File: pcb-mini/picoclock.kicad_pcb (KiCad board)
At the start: 2 copper layers, 140 x 54 mm, 123 parts, among them J1 UART, J10 USB, J11 Alt Power, J12 LED_5V, J14 SM03B-SRSS-TB, J15 Conn_01x24, J2 USB_A, J4 xx, J5 Micro_SD_Card_Det1, J6 USB_C_Receptacle, J9 AUDIO, Q1 BSS138, Q3 BSS138, SW1 SW_Push, SW2 SW_Push, SW3 SW_Push, SW4 SW_Push, SW5 SW_Push, SW6 SW_Push, SW7 SW_Push, SW8 SW_Push, U1 PCF8563T, U2 RP2350_80QFN, U3 MCP9808_MSOP, U4 PCM5100, U5 PAM8302A, U7 MCP45X1-104E, U8 NCP1117-3.3_SOT223, U9 ESP32-WROOM-E, Y1 Crystal, Y2 ABM8-272-T3

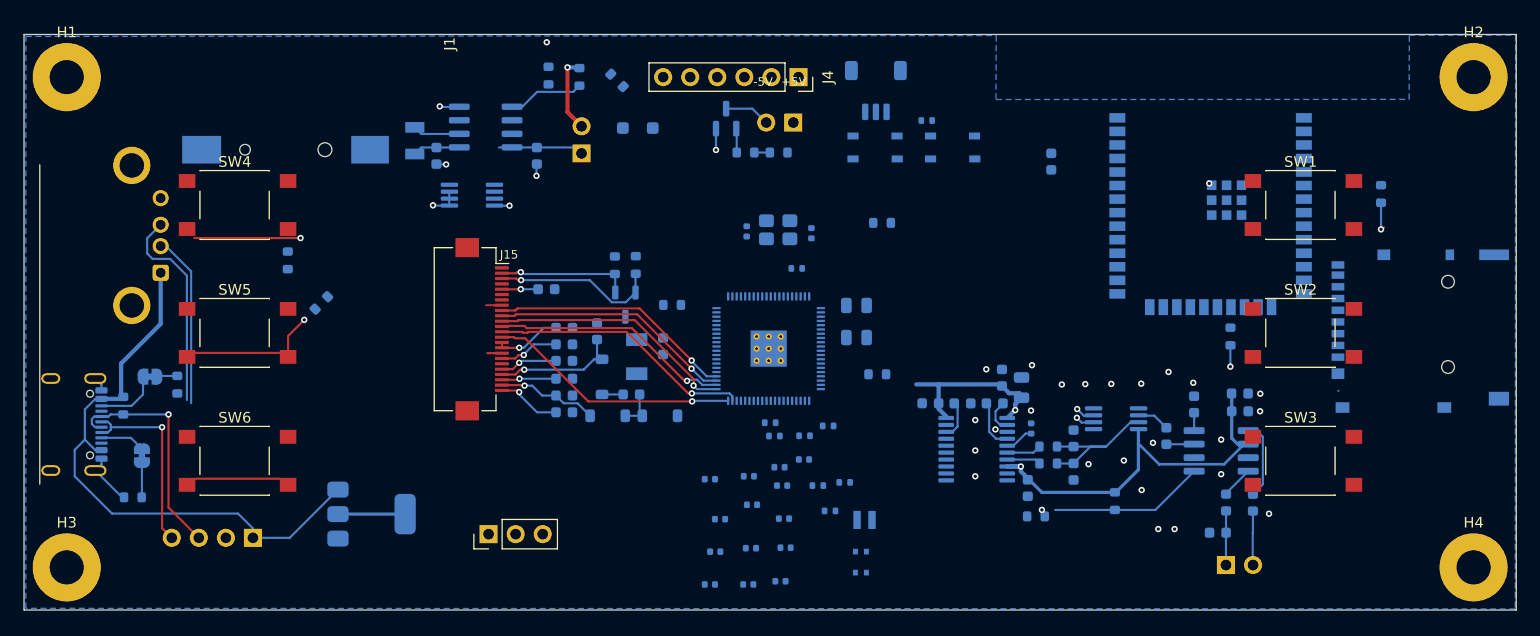
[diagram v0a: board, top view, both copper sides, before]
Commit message: [pcb-mini] add ESP32, RM2, route most things
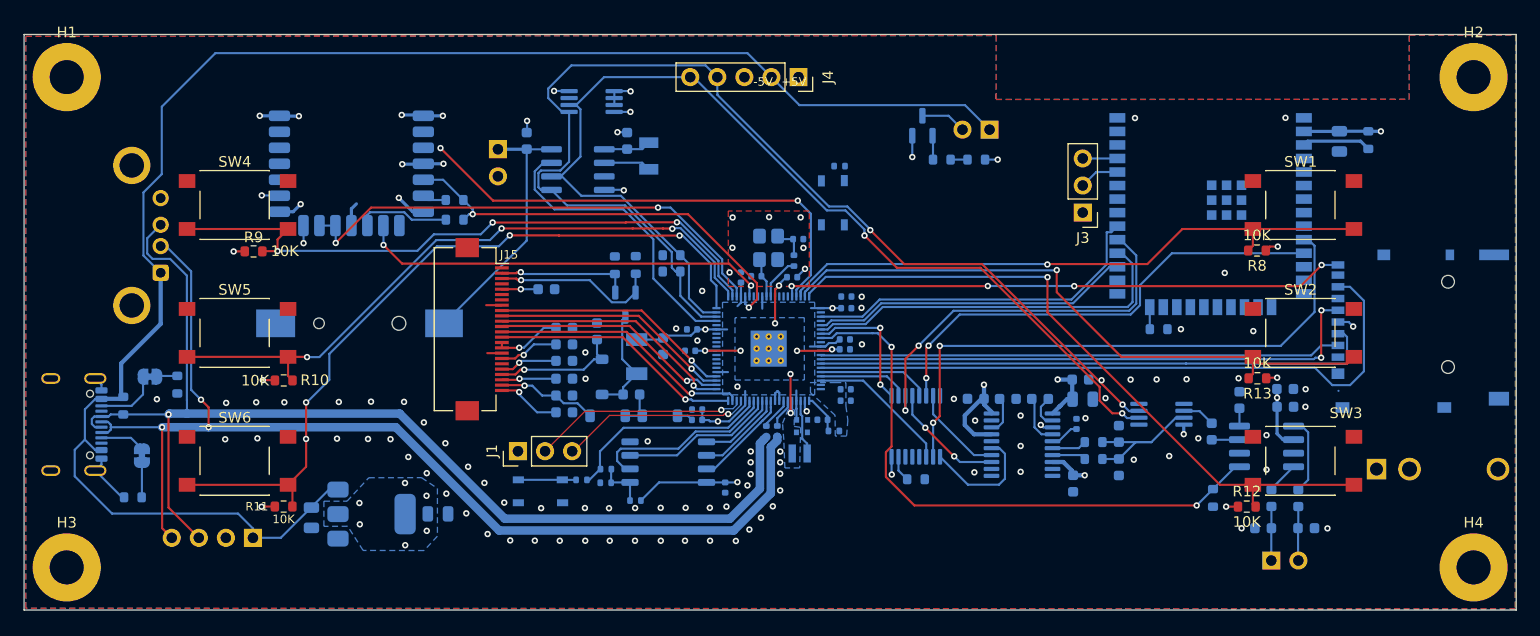
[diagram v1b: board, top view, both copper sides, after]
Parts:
- removed D1: 1A 20V Schottky, Diode_SMD:D_SOD-123F
- removed J14: SM03B-SRSS-TB, Connector_JST:JST_SH_SM03B-SRSS-TB_1x03-1MP_P1.00mm_Horizontal
- removed the R1 at (132.1, 84.0)
- removed the R17 at (160.5, 97.7)
- removed the R17 at (150.8, 91.1)
- removed the R3 at (135.6, 84.3)
- added C48: 10u, Capacitor_SMD:C_0805_2012Metric, B.Cu at (203.4, 90.0)
- added J3: UART, Connector_PinHeader_2.54mm:PinHeader_1x03_P2.54mm_Vertical, F.Cu at (179.3, 96.7)
- added J7: AudioJack2_Ground, Connector_Audio:Jack_3.5mm_QingPu_WQP-PJ398SM_Vertical_CircularHoles, B.Cu at (206.9, 120.8)
- added J8: Conn_01x21_Pin, RMC20452T:RMC20452T, B.Cu at (110.7, 90.2)
- added R17: 10K, Resistor_SMD:R_0603_1608Metric, B.Cu at (169.3, 91.7)
- added R28: 10K, Resistor_SMD:R_0603_1608Metric, B.Cu at (186.4, 107.7)
- added R29: 10K, Resistor_SMD:R_0603_1608Metric, B.Cu at (206.1, 89.9)
- added R30: 10K, Resistor_SMD:R_0603_1608Metric, B.Cu at (163.7, 121.7)
- added R37: 470, Resistor_SMD:R_0603_1608Metric, B.Cu at (120.4, 95.5)
- added R38: 10k, Resistor_SMD:R_0603_1608Metric, B.Cu at (120.4, 97.4)
- added U10: 74LS157, Package_SO:TSSOP-16_4.4x5mm_P0.65mm, B.Cu at (163.7, 116.8)
- added U6: W25Q128JVS, Package_SO:SOIC-8_5.3x5.3mm_P1.27mm, B.Cu at (140.4, 120.1)
- J4: footprint Connector_PinSocket_2.54mm:PinSocket_1x06_P2.54mm_Vertical -> Connector_PinSocket_2.54mm:PinSocket_1x05_P2.54mm_Vertical
- R10, R11, R12, R13, R8, R9: moved to F.Cu
- moved C46 53.9 mm to (107.0, 125.3), turned to -90 degrees
- moved SW7 50.4 mm to (128.4, 122.9)
- moved R11 47.5 mm to (104.3, 124.3), turned to 0 degrees
- moved R15 46.8 mm to (132.3, 121.8), turned to 180 degrees
- moved C47 43.9 mm to (118.8, 125.0)
- moved C30 41.9 mm to (200.3, 126.3), turned to 0 degrees
- moved C40 28.7 mm to (147.3, 102.8), turned to 90 degrees
- moved R18 24.4 mm to (156.5, 92.3)
- moved C38 24.2 mm to (157.1, 105.7)
- moved C34 23.8 mm to (157.0, 109.5)
- moved Y1 22.0 mm to (138.6, 91.4), turned to -90 degrees
- moved C44 21.6 mm to (157.2, 104.6)
- moved R1 21.6 mm to (140.7, 102.2)
- moved R23 21.4 mm to (134.6, 120.8)
- moved R20 19.9 mm to (134.6, 122.1)
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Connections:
- net GPIO1 renamed GPIO1_RX
- J1 pad 3: GPIO0 -> GPIO0_TX
- J4 pad 4: LED_5V- -> SDA
- J4 pad 5: SDA -> SCL
- R20 pad 1: GPIO0 -> /uC/GPIO0
- U2 pad 11: SD_D0_MISO -> unconnected-(U2-GPIO12-Pad11)
- U2 pad 12: SD_D3_CS -> unconnected-(U2-GPIO13-Pad12)
- U2 pad 13: SD_CLK -> unconnected-(U2-GPIO14-Pad13)
- U2 pad 14: SD_CMD_MOSI -> unconnected-(U2-GPIO15-Pad14)
- U2 pad 22: DIN -> GPIO28/btn
- U2 pad 23: MUTE -> RM2_BT_ON
- U2 pad 25: SD_DET -> RM2_SPI_IRQ
- U2 pad 26: unconnected-(U2-GPIO25-Pad26) -> RM2_SPI_CS
- U2 pad 27: BCK -> unconnected-(U2-GPIO26-Pad27)
- U2 pad 28: LRCK -> unconnected-(U2-GPIO27-Pad28)
- U2 pad 36: GPIO28/btn -> SD_DET
- U2 pad 37: GPE7/led -> RM2_SPI_CLK_GP29
- U2 pad 38: unconnected-(U2-GPIO30-Pad38) -> GPIO8/btn
- U2 pad 39: unconnected-(U2-GPIO31-Pad39) -> GPIO9/btn
- U2 pad 40: unconnected-(U2-GPIO32-Pad40) -> GPIO10/btn
- U2 pad 43: unconnected-(U2-GPIO34-Pad43) -> GPIO34_ESP32_COM
- U2 pad 45: unconnected-(U2-GPIO36-Pad45) -> ESP32_UART1_RX
- U2 pad 46: unconnected-(U2-GPIO37-Pad46) -> ESP32_UART1_TX
- U2 pad 47: unconnected-(U2-GPIO38-Pad47) -> GPIO35_I2S_SELECT
- U2 pad 48: unconnected-(U2-GPIO39-Pad48) -> MUTE
- U2 pad 52: unconnected-(U2-GPIO41_ADC1-Pad52) -> SD_D3_CS
- U2 pad 53: unconnected-(U2-GPIO42_ADC2-Pad53) -> SD_CLK
- U2 pad 54: unconnected-(U2-GPIO43_ADC3-Pad54) -> SD_CMD_MOSI
- U2 pad 55: unconnected-(U2-GPIO44_ADC4-Pad55) -> SD_D0_MISO
- U2 pad 56: unconnected-(U2-GPIO45_ADC5-Pad56) -> PICO_DIN
- U2 pad 57: unconnected-(U2-GPIO46_ADC6-Pad57) -> PICO_BCK
- U2 pad 58: unconnected-(U2-GPIO47_ADC7-Pad58) -> PICO_LRCK
- U2 pad 6: GPIO8/btn -> unconnected-(U2-GPIO8-Pad6)
- U2 pad 7: GPIO9/btn -> unconnected-(U2-GPIO9-Pad7)
- U2 pad 77: GPIO0 -> GPIO0_TX
- U2 pad 8: GPIO10/btn -> unconnected-(U2-GPIO10-Pad8)
- U9 pad 10: unconnected-(U9-DAC_1/ADC2_CH8/GPIO25-Pad10) -> BT_I2S_LRCK
- U9 pad 11: unconnected-(U9-DAC_2/ADC2_CH9/GPIO26-Pad11) -> BT_I2S_SDATA
- U9 pad 24: unconnected-(U9-ADC2_CH2/GPIO2-Pad24) -> ESP32_IO2
- U9 pad 25: unconnected-(U9-GPIO0/BOOT/ADC2_CH1-Pad25) -> ESP32_IO0
- U9 pad 27: unconnected-(U9-GPIO16-Pad27) -> ESP32_UART1_RX
- U9 pad 28: unconnected-(U9-GPIO17-Pad28) -> ESP32_UART1_TX
- U9 pad 29: unconnected-(U9-GPIO5-Pad29) -> BT_I2S_SCK
- U9 pad 3: unconnected-(U9-EN/CHIP_PU-Pad3) -> ESP32_EN
- U9 pad 30: unconnected-(U9-GPIO18-Pad30) -> GPIO34_ESP32_COM
- U9 pad 34: unconnected-(U9-U0RXD/GPIO3-Pad34) -> ESP32_UART0_RX
- U9 pad 35: unconnected-(U9-U0TXD/GPIO1-Pad35) -> ESP32_UART0_TX
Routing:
- net LED_5V+: track 55.3 -> 155.0 mm
- net SDA: track 9.45 -> 107.9 mm, vias 1 -> 2
- net SCL: track 1.73 -> 100.0 mm, vias 1 -> 2
- net USB D-: track 34.2 -> 105.3 mm, vias 1 -> 3
- net USB D+: track 41.1 -> 108.3 mm
- net GPIO10/btn: track 0.00 -> 64.2 mm, vias 0 -> 1
- net GPIO20/btn: track 7.96 -> 71.5 mm, vias 0 -> 4
- net SD_D0_MISO: track 0.00 -> 61.8 mm
- net GPIO28/btn: track 0.00 -> 61.3 mm, vias 0 -> 3
- net GPIO9/btn: track 2.42 -> 60.1 mm
- net BT_I2S_LRCK: track 0.00 -> 54.6 mm, vias 0 -> 2
- net GPIO8/btn: track 2.60 -> 57.0 mm
- net SD_DET: track 0.00 -> 53.1 mm, vias 0 -> 4
- net SD_CLK: track 0.00 -> 53.0 mm, vias 0 -> 2
- net SD_CMD_MOSI: track 0.00 -> 52.8 mm
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- added copper zone on B.Cu, net +1V1
- added copper zone on B.Cu, net +3V3
- added copper zone on In2.Cu, net +3V3
- added copper zone on F.Cu, net GND
- added copper zone on In1.Cu, net GND
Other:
- outline, holes or cut-outs redrawn
- copper layers 2 -> 4

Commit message: [pcb-mini] fix warnings/errors
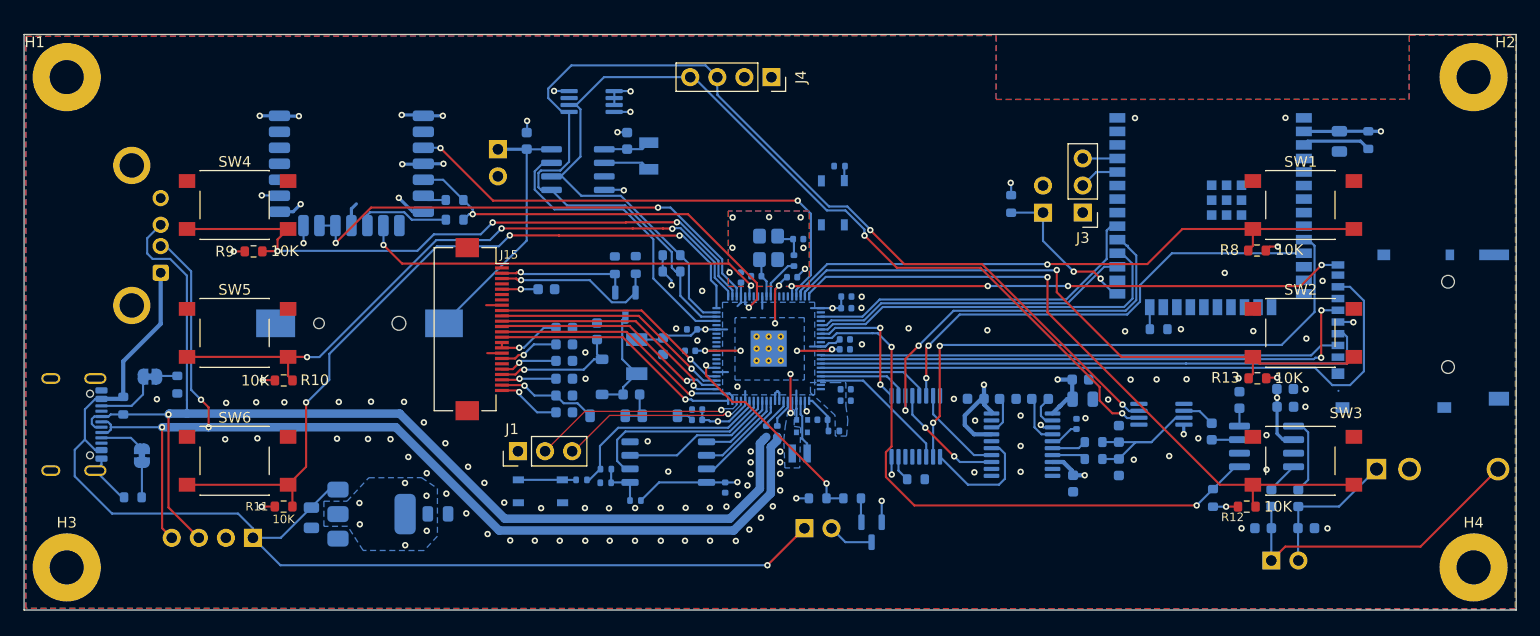
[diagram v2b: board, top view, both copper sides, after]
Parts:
- added J13: ESP32_IO0, Connector_PinHeader_2.54mm:PinHeader_1x02_P2.54mm_Vertical, B.Cu at (175.6, 96.7)
- added R31: 10K, Resistor_SMD:R_0603_1608Metric, B.Cu at (172.6, 95.9)
- J4: footprint Connector_PinSocket_2.54mm:PinSocket_1x05_P2.54mm_Vertical -> Connector_PinSocket_2.54mm:PinSocket_1x04_P2.54mm_Vertical
- moved J12 41.2 mm to (153.2, 126.3), turned to -90 degrees
- moved Q1 38.4 mm to (159.5, 126.7), turned to -90 degrees
- moved R17 35.1 mm to (154.5, 123.5), turned to 0 degrees
- moved R19 32.9 mm to (157.7, 123.5), turned to 0 degrees
- moved J4 2.54 mm to (150.1, 84.0)
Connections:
- J4 pad 2: LED_5V+ -> +3V3
- J4 pad 3: +3V3 -> SDA
- J4 pad 4: SDA -> SCL
- R19 pad 1: GPE7/led -> SCREEN_LED
- U2 pad 6: unconnected-(U2-GPIO8-Pad6) -> SCREEN_LED
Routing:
- net LED_5V+: track 155.0 -> 109.6 mm, vias 0 -> 1
- net MONO_OUT_R-: track 5.08 -> 29.9 mm
- net SCREEN_LED: track 0.00 -> 20.5 mm, vias 0 -> 2
- net ESP32_IO0: track 0.00 -> 14.8 mm, vias 0 -> 2
- net MONO_OUT_R+: track 5.09 -> 13.9 mm
- net +3V3: track 89.6 -> 96.1 mm, vias 29 -> 31
- net RM2_SPI_CLK_GP29: track 45.6 -> 47.2 mm
- net GPE7/led: track 1.58 -> 0.00 mm
- net Net-(R18-Pad1): track 0.00 -> 1.38 mm
- net GND: track 43.2 -> 41.8 mm, vias 111 -> 116
- net +1V1: track 20.3 -> 21.4 mm
- net /uC/QSPI_SD1: track 17.5 -> 18.2 mm
- net GPIO20/btn: vias 4 -> 3
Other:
- board text added: "+3.3V"
- board text added: "- + 5V"
- board text added: "RX"
- board text added: "SCL"
- board text added: "SDA"
- board text added: "TX"
- board text removed: "-5V"

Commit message: [3d] add mini case
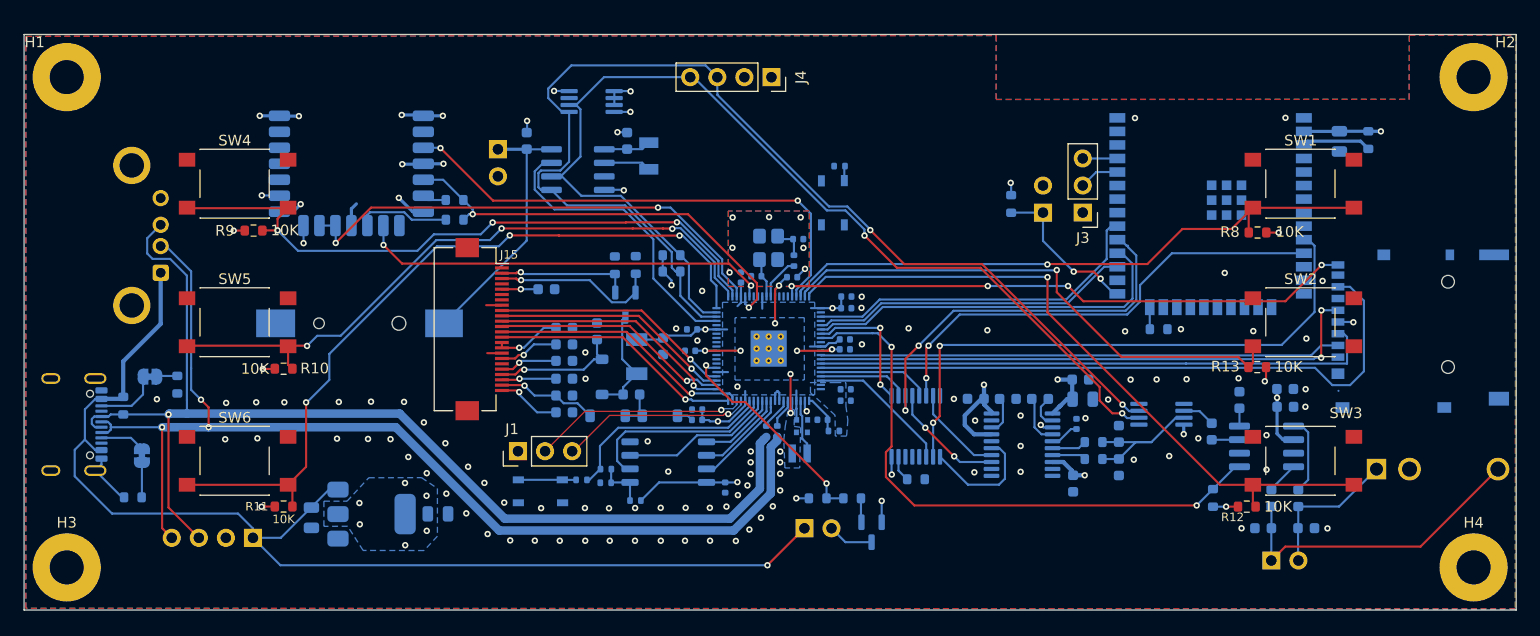
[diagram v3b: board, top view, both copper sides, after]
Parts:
- moved SW1 2.00 mm to (200.0, 94.0)
- moved SW4 2.00 mm to (100.0, 94.0)
- moved R9 1.95 mm to (101.5, 98.4)
- moved R8 1.69 mm to (195.7, 98.6)
- moved R10 1.10 mm to (104.3, 111.4)
- moved R13 1.05 mm to (195.7, 111.2)
- moved SW2 1.00 mm to (200.0, 107.0)
- moved SW5 1.00 mm to (100.0, 107.0)
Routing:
- net GPIO9/btn: track 60.1 -> 50.0 mm
- net SD_DET: track 53.1 -> 54.3 mm
- net GPIO8/btn: track 57.0 -> 58.2 mm
- net GPIO28/btn: track 61.3 -> 62.4 mm

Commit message: [mini] add pin for screen holder in pcb + 3d
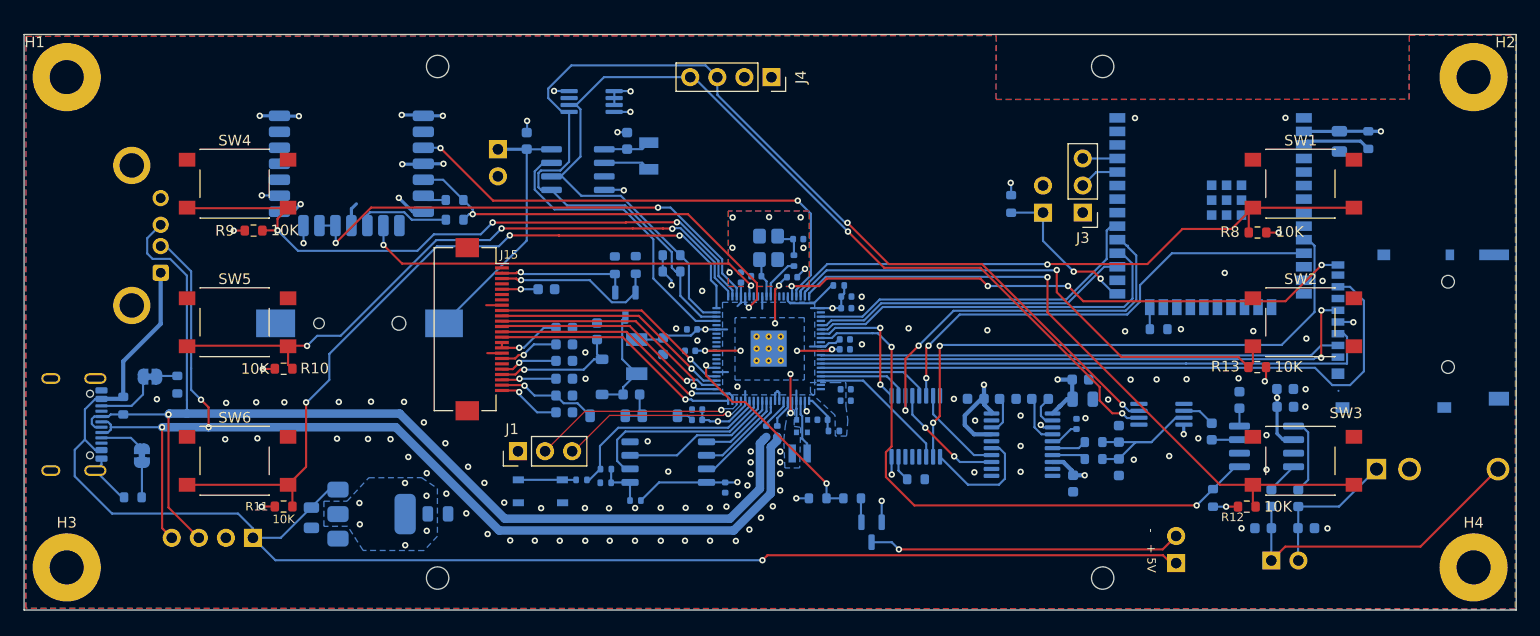
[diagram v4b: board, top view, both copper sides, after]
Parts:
- removed SW8: SW_Push, Button_Switch_SMD:SW_Push_1P1T_NO_Vertical_Wuerth_434133025816
- moved J12 35.0 mm to (188.1, 129.6), turned to 0 degrees
- moved R18 11.2 mm to (156.4, 103.5), turned to 0 degrees
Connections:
- R18 pad 1: Net-(R18-Pad1) -> /uC/RUN
- R18 pad 2: GND -> +3V3
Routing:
- net LED_5V+: track 109.6 -> 143.3 mm
- net LED_5V-: track 3.71 -> 29.4 mm, vias 0 -> 1
- net /uC/RUN: track 0.00 -> 5.48 mm
- net Net-(R18-Pad1): track 1.38 -> 0.00 mm
- net +3V3: track 96.4 -> 97.5 mm
- net SD_DET: track 54.3 -> 54.8 mm
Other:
- outline, holes or cut-outs redrawn

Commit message: [pcb-mini] add proper audio jack
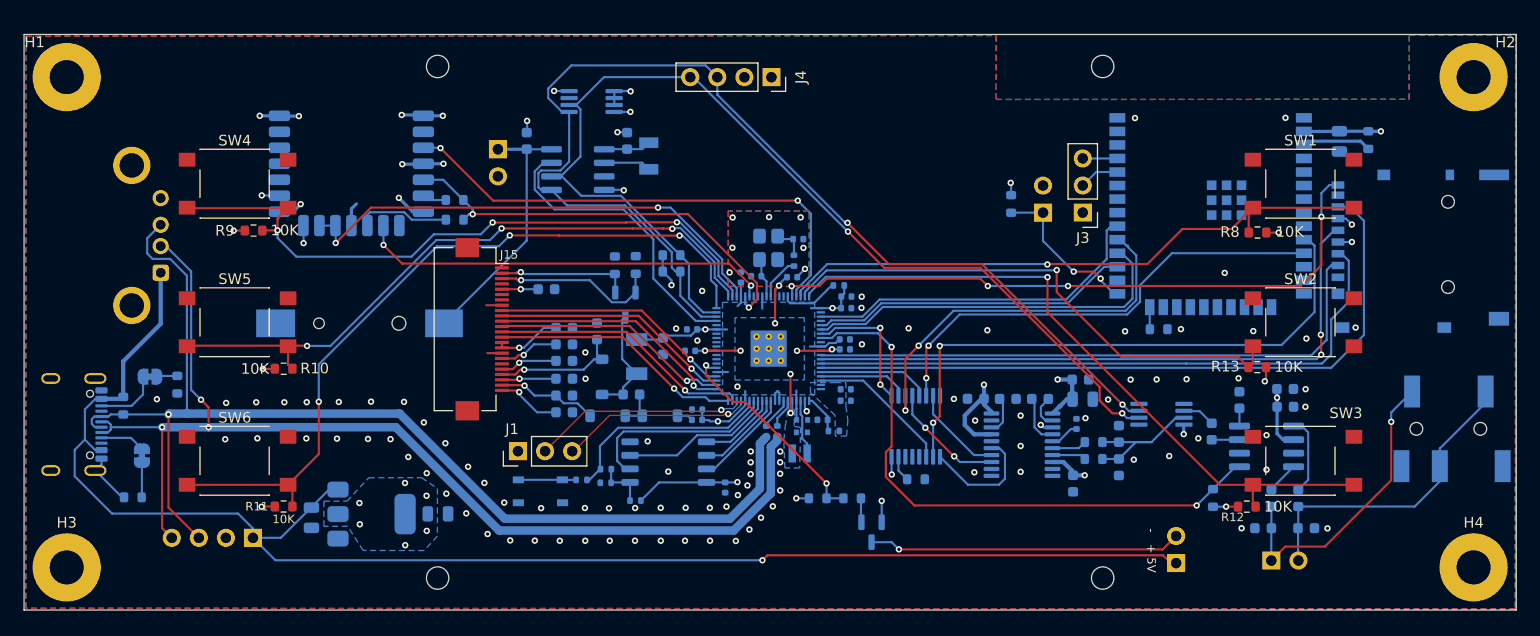
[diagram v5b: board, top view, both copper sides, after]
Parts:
- removed J7: AudioJack2_Ground, Connector_Audio:Jack_3.5mm_QingPu_WQP-PJ398SM_Vertical_CircularHoles
- added J14: SJ2-35863B1-SMT-TR, SJ2-35863B1-SMT-TR:CUI_SJ2-35863B1-SMT-TR, B.Cu at (213.6, 117.0)
- moved J5 7.50 mm to (211.0, 100.0)
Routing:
- net MONO_OUT_R+: track 13.9 -> 29.6 mm
- net SD_D3_CS: track 48.9 -> 55.9 mm
- net SD_CLK: track 53.0 -> 59.7 mm
- net SD_CMD_MOSI: track 52.8 -> 59.0 mm
- net SD_DET: track 54.8 -> 60.7 mm
- net SD_D0_MISO: track 61.8 -> 65.9 mm
- net GND: track 41.8 -> 43.3 mm, vias 116 -> 119
- net MONO_OUT_R-: track 29.9 -> 28.6 mm, vias 0 -> 1
- net GPIO28/btn: track 62.4 -> 63.3 mm
